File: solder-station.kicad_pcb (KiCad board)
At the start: 2 copper layers, 46 parts, among them J1 Temp Sensor, J2 Heating Element, J3 SWD ISP, J4 STM_UART, Q1 MBT3946DW1T1, Q2 MBT3946DW1T1, Q3 L2N7002M3T5G, Q4 L2N7002M3T5G, Q5 FDMS6681Z, U1 LM75B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

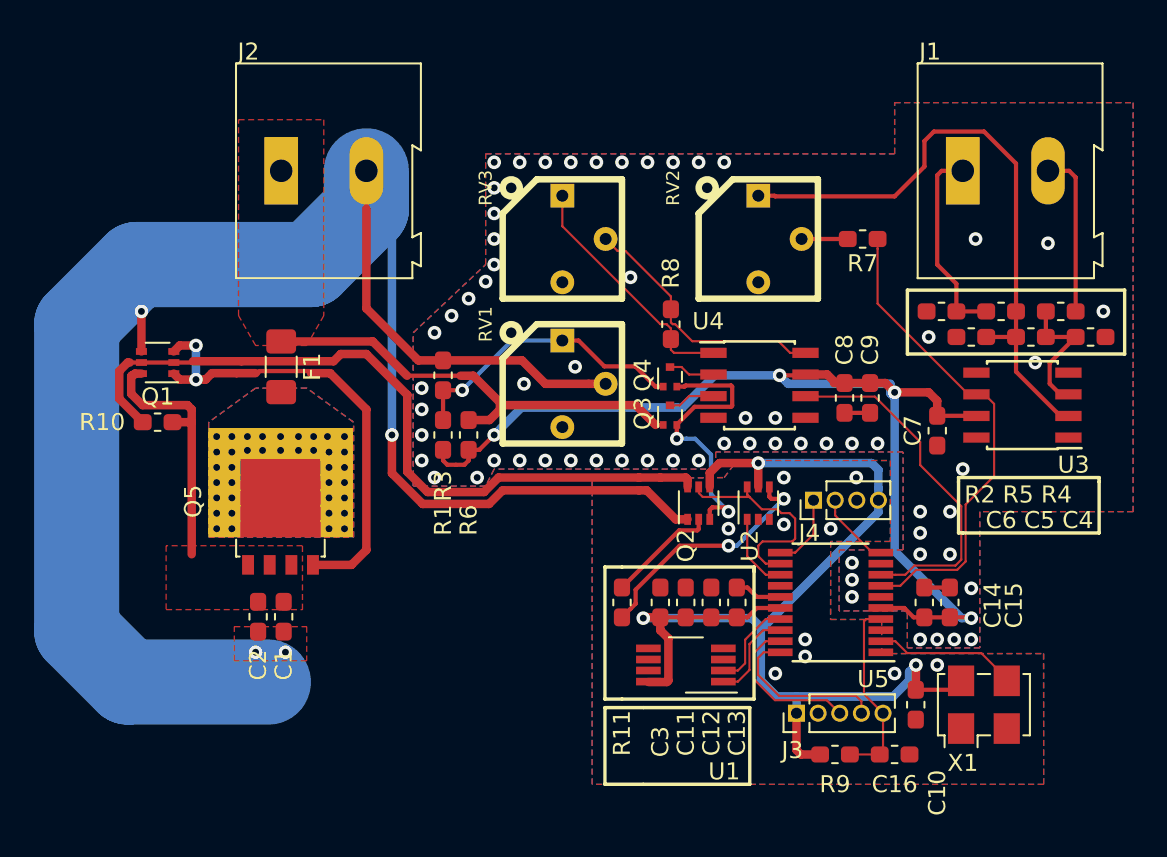
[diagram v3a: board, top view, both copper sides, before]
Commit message: Add power supplies
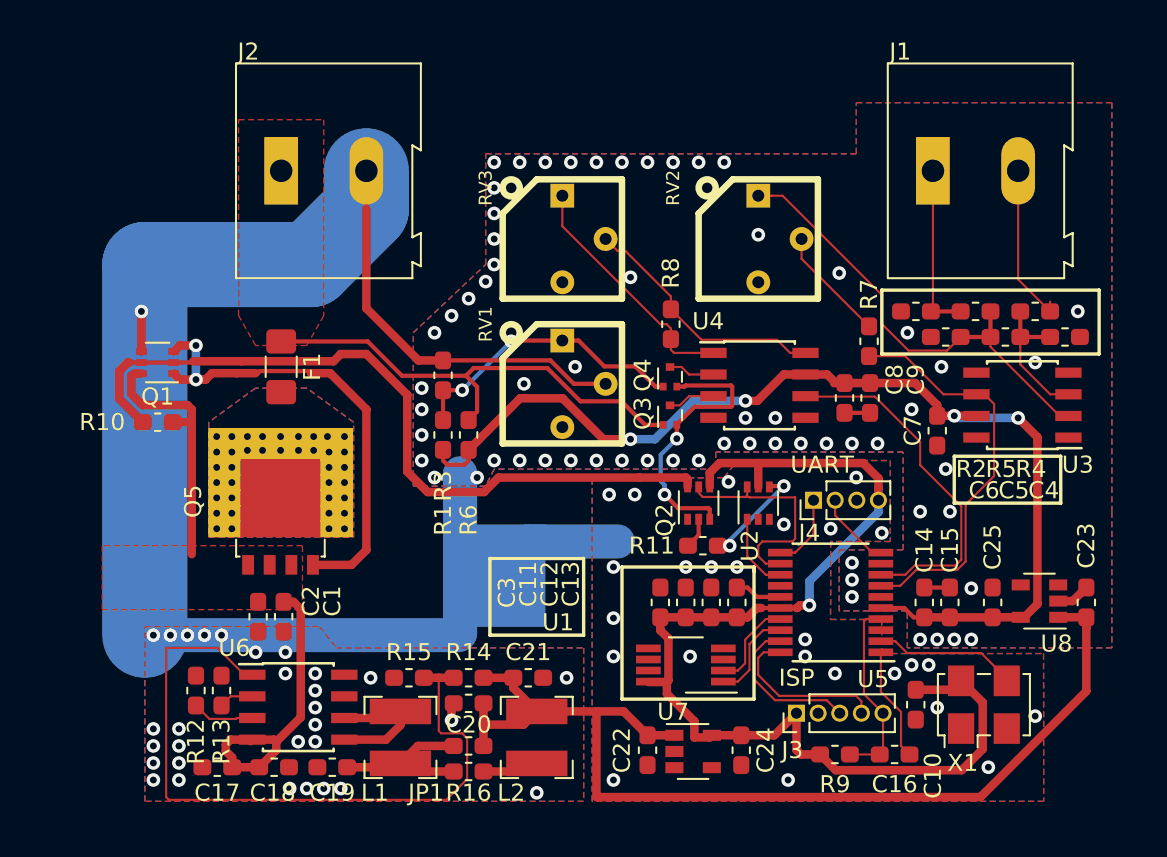
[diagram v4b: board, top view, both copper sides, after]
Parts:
- added C17: 47u, Capacitor_SMD:C_0603_1608Metric_Pad1.05x0.95mm_HandSolder, F.Cu at (80.2, 87.5)
- added C18: 47u, Capacitor_SMD:C_0603_1608Metric_Pad1.05x0.95mm_HandSolder, F.Cu at (83.6, 87.5)
- added C19: 47u, Capacitor_SMD:C_0603_1608Metric_Pad1.05x0.95mm_HandSolder, F.Cu at (87.0, 87.5)
- added C20: 47u, Capacitor_SMD:C_0603_1608Metric_Pad1.05x0.95mm_HandSolder, F.Cu at (95.0, 83.8)
- added C21: 47u, Capacitor_SMD:C_0603_1608Metric_Pad1.05x0.95mm_HandSolder, F.Cu at (98.5, 82.2)
- added C22: 1u, Capacitor_SMD:C_0603_1608Metric_Pad1.05x0.95mm_HandSolder, F.Cu at (105.5, 86.5)
- added C23: 1u, Capacitor_SMD:C_0603_1608Metric_Pad1.05x0.95mm_HandSolder, F.Cu at (131.2, 77.8)
- added C24: 1u, Capacitor_SMD:C_0603_1608Metric_Pad1.05x0.95mm_HandSolder, F.Cu at (111.0, 86.5)
- added C25: 1u, Capacitor_SMD:C_0603_1608Metric_Pad1.05x0.95mm_HandSolder, F.Cu at (125.8, 77.8)
- added JP1: SolderJumper_2_Open, Resistor_SMD:R_0603_1608Metric_Pad1.05x0.95mm_HandSolder, F.Cu at (95.0, 86.2)
- added L1: 4.7u, Inductor_SMD:L_Bourns-SRN4018, F.Cu at (91.0, 85.8)
- added L2: 4.7u, Inductor_SMD:L_Bourns-SRN4018, F.Cu at (99.0, 85.8)
- added NT1: Net-Tie_4, NetTie:NetTie-4_SMD_Pad2.0mm, B.Cu at (96.5, 76.2)
- added R12: 27k, Resistor_SMD:R_0603_1608Metric_Pad1.05x0.95mm_HandSolder, F.Cu at (79.0, 83.0)
- added R13: 120k, Resistor_SMD:R_0603_1608Metric_Pad1.05x0.95mm_HandSolder, F.Cu at (80.5, 83.0)
- added R14: 475k, Resistor_SMD:R_0603_1608Metric_Pad1.05x0.95mm_HandSolder, F.Cu at (95.0, 82.2)
- added R15: 150k, Resistor_SMD:R_0603_1608Metric_Pad1.05x0.95mm_HandSolder, F.Cu at (91.5, 82.2)
- added R16: 150m, Resistor_SMD:R_0603_1608Metric_Pad1.05x0.95mm_HandSolder, F.Cu at (95.0, 87.8)
- added U6: FM1613, Package_SO:SOIC-8_3.9x4.9mm_P1.27mm, F.Cu at (85.0, 84.0)
- added U7: XC6201P332, Package_TO_SOT_SMD:SOT-23-5, F.Cu at (108.2, 86.6)
- added U8: XC6201P332, Package_TO_SOT_SMD:SOT-23-5, F.Cu at (128.5, 77.8)
- R3: value DNP -> 3.3
- moved R7 6.01 mm to (118.5, 62.5), turned to 90 degrees
- moved R11 5.80 mm to (108.8, 74.5), turned to 0 degrees
- moved J1 1.75 mm to (122.2, 52.5)
- moved C4 1.50 mm to (130.0, 62.2)
- moved C5 1.50 mm to (126.5, 62.2)
- moved C6 1.50 mm to (123.0, 62.2)
- moved R2 1.50 mm to (121.2, 60.8)
- moved R4 1.50 mm to (128.2, 60.8)
- moved R5 1.50 mm to (124.8, 60.8)
- turned C3 to 90 degrees
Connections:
- C1 pad 2: GNDPWR -> GND
- C10 pad 2: GND -> GNDD
- C11 pad 2: GND -> GNDD
- C12 pad 2: GND -> GNDD
- C13 pad 2: GND -> GNDD
- C16 pad 2: GND -> Net-(C16-Pad2)
- C2 pad 2: GNDPWR -> GND
- C3 pad 1: GND -> +3V3
- C3 pad 2: +3V3 -> GNDD
- J2 pad 2: GNDPWR -> GND
- J3 pad 2: GND -> GNDD
- J4 pad 3: GND -> GNDD
- Q1 pad 4: GNDPWR -> GND
- Q2 pad 1: GNDPWR -> GNDD
- R3 pad 2: GNDPWR -> GND
- RV1 pad 2: GNDPWR -> GND
- U1 pad 4: GND -> GNDD
- U1 pad 5: GND -> GNDD
- U1 pad 6: GND -> GNDD
- U1 pad 7: GND -> GNDD
- U2 pad 2: GND -> GNDD
- U2 pad 3: GND -> GNDD
- U5 pad 1: GND -> Net-(C16-Pad2)
- U5 pad 15: GND -> GNDD
- X1 pad 2: GND -> GNDD
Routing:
- net GNDPWR: track 117.5 -> 0.00 mm, vias 4 -> 0
- net GND: track 3.28 -> 85.4 mm, vias 10 -> 31
- net +5V: track 0.00 -> 61.3 mm
- net Net-(R14-Pad1): track 0.00 -> 41.8 mm
- net +24V: track 15.3 -> 33.1 mm
- net Net-(C19-Pad1): track 0.00 -> 10.1 mm
- net Net-(C5-Pad2): track 36.5 -> 27.0 mm
- net GNDD: track 0.00 -> 8.03 mm, vias 0 -> 25
- net Net-(R11-Pad2): track 14.5 -> 6.53 mm
- net Net-(L1-Pad2): track 0.00 -> 7.91 mm
- net Net-(C16-Pad2): track 0.00 -> 7.19 mm
- net GNDA: track 3.00 -> 8.98 mm, vias 64 -> 63
- net Net-(Q2-Pad2): track 6.50 -> 1.81 mm
- net /A_THERMO: track 28.6 -> 24.0 mm
- net Net-(R7-Pad2): track 2.71 -> 6.77 mm
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- added copper zone on B.Cu, net GNDD
- added copper zone on F.Cu, net GNDD
- removed copper zone on F.Cu, net GNDPWR
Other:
- board text added: "ISP"
- board text added: "UART"

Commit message: Move some things around
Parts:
- added J5: Power, TerminalBlock_MetzConnect:TerminalBlock_MetzConnect_Type011_RT05502HBWC_1x02_P5.00mm_Horizontal, F.Cu at (65.2, 70.5)
- J1: footprint TerminalBlock:TerminalBlock_Altech_AK300-2_P5.00mm -> Connector_PinHeader_1.27mm:PinHeader_1x02_P1.27mm_Vertical
- J2: footprint TerminalBlock:TerminalBlock_Altech_AK300-2_P5.00mm -> TerminalBlock_MetzConnect:TerminalBlock_MetzConnect_Type011_RT05502HBWC_1x02_P5.00mm_Horizontal
- J3: value SWD ISP -> ISP
- J4: value STM_UART -> I2C
- NT1: value Net-Tie_4 -> Star Ground
- moved C22 20.3 mm to (97.8, 67.8)
- moved C24 20.3 mm to (103.2, 67.8)
- moved U7 20.3 mm to (100.4, 67.8)
- moved J4 18.2 mm to (100.0, 81.8)
- moved C16 12.7 mm to (110.8, 78.0), turned to 180 degrees
- moved R9 11.8 mm to (110.8, 76.5)
- moved C10 8.88 mm to (113.7, 79.1)
- moved X1 8.88 mm to (117.7, 79.1)
- moved C23 8.87 mm to (124.5, 72.1)
- moved C25 8.87 mm to (119.0, 72.1)
- moved U8 8.87 mm to (121.8, 72.0)
- moved J3 8.40 mm to (106.2, 81.8)
- moved Q3 8.13 mm to (101.1, 61.1)
- moved Q4 8.13 mm to (101.1, 58.8)
- moved U4 8.13 mm to (106.3, 59.3)
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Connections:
- C16 pad 2: Net-(C16-Pad2) -> GNDD
- J4 pad 1: /USART6_RX -> +3V3
- J4 pad 2: /USART6_TX -> GNDD
- J4 pad 3: GNDD -> /I2C1_SCL
- J4 pad 4: +3V3 -> /I2C1_SDA
- U5 pad 1: Net-(C16-Pad2) -> GNDD
- U5 pad 10: /USART6_TX -> GNDA
- U5 pad 11: /USART6_RX -> GNDD
- U5 pad 14: Net-(U5-Pad14) -> GNDD
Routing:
- net GND: track 85.4 -> 67.1 mm
- net +5V: track 61.3 -> 69.3 mm
- net Net-(C16-Pad2): track 7.19 -> 0.00 mm
- net /I2C1_SCL: track 5.40 -> 12.3 mm
- net /I2C1_SDA: track 5.49 -> 11.6 mm
- net Net-(J1-Pad2): track 9.60 -> 3.84 mm
- net Net-(Q1-Pad2): track 44.3 -> 49.8 mm, vias 0 -> 2
- net Net-(R11-Pad2): track 6.53 -> 1.64 mm, vias 2 -> 0
- net /USART6_TX: track 4.48 -> 0.00 mm
- net /USART6_RX: track 4.40 -> 0.00 mm
- net Net-(J1-Pad1): track 10.6 -> 6.39 mm
- net /EN_PWR: track 4.56 -> 7.80 mm
- net /EN_SEN: track 13.7 -> 10.6 mm
- net +3V3: track 68.3 -> 66.7 mm, vias 1 -> 2
- net +3.3VA: track 63.4 -> 61.8 mm
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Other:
- board outline added: 100 x 100 mm
- board text added: "24V"
- board text added: "I2C"
- board text added: "Iron"
- board text added: "TC"
- board text removed: "UART"

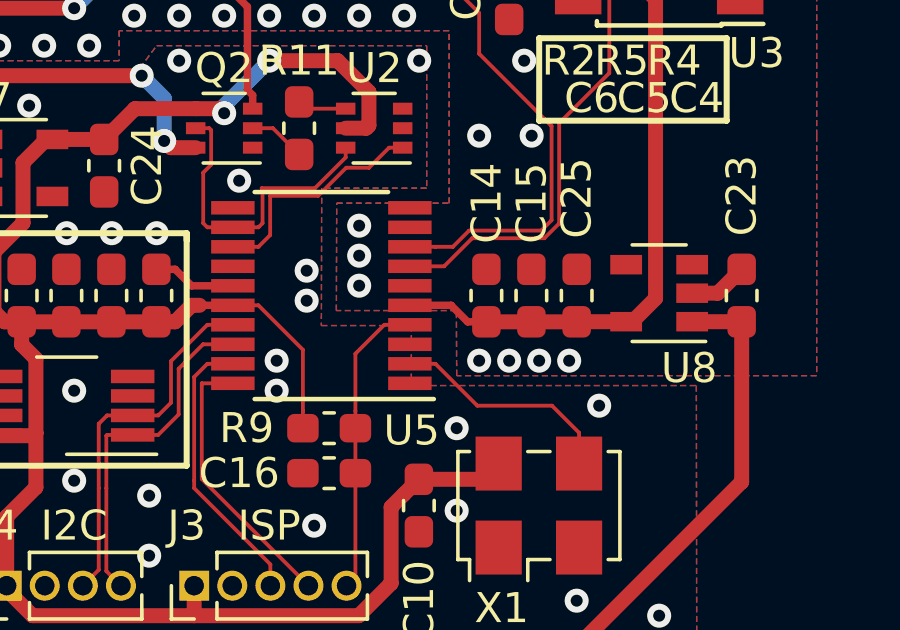
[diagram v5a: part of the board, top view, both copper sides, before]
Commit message: Add test points
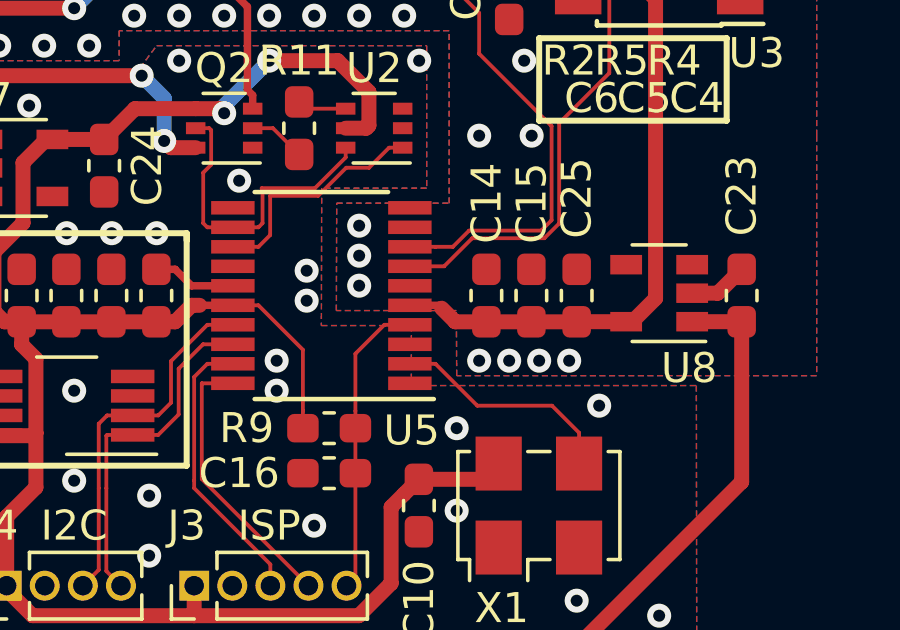
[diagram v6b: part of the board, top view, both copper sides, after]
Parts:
- C14, C7, C8: value 10n -> .1u

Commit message: Misc changes
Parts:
- moved C16 54.7 mm to (64.2, 49.2)
- moved C17 54.7 mm to (28.0, 53.0)
- moved C18 54.7 mm to (31.3, 53.0)
- moved C19 54.7 mm to (34.8, 53.0)
- moved C20 54.7 mm to (42.8, 49.2)
- moved C21 54.7 mm to (46.2, 47.8)
- moved C22 54.7 mm to (51.2, 39.0)
- moved C24 54.7 mm to (56.8, 39.0)
- moved C4 54.7 mm to (77.8, 27.8)
- moved C5 54.7 mm to (74.2, 27.8)
- moved C6 54.7 mm to (70.8, 27.8)
- moved C7 54.7 mm to (70.2, 33.2)
- moved C8 54.7 mm to (64.8, 31.3)
- moved C9 54.7 mm to (66.3, 31.3)
- moved F1 54.7 mm to (31.8, 29.5)
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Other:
- board size 100 x 100 mm -> 85 x 100 mm
